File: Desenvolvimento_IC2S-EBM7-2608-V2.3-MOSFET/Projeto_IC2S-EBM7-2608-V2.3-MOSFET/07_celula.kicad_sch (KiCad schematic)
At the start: 23 parts, among them U13 LP5907MFX-2.5

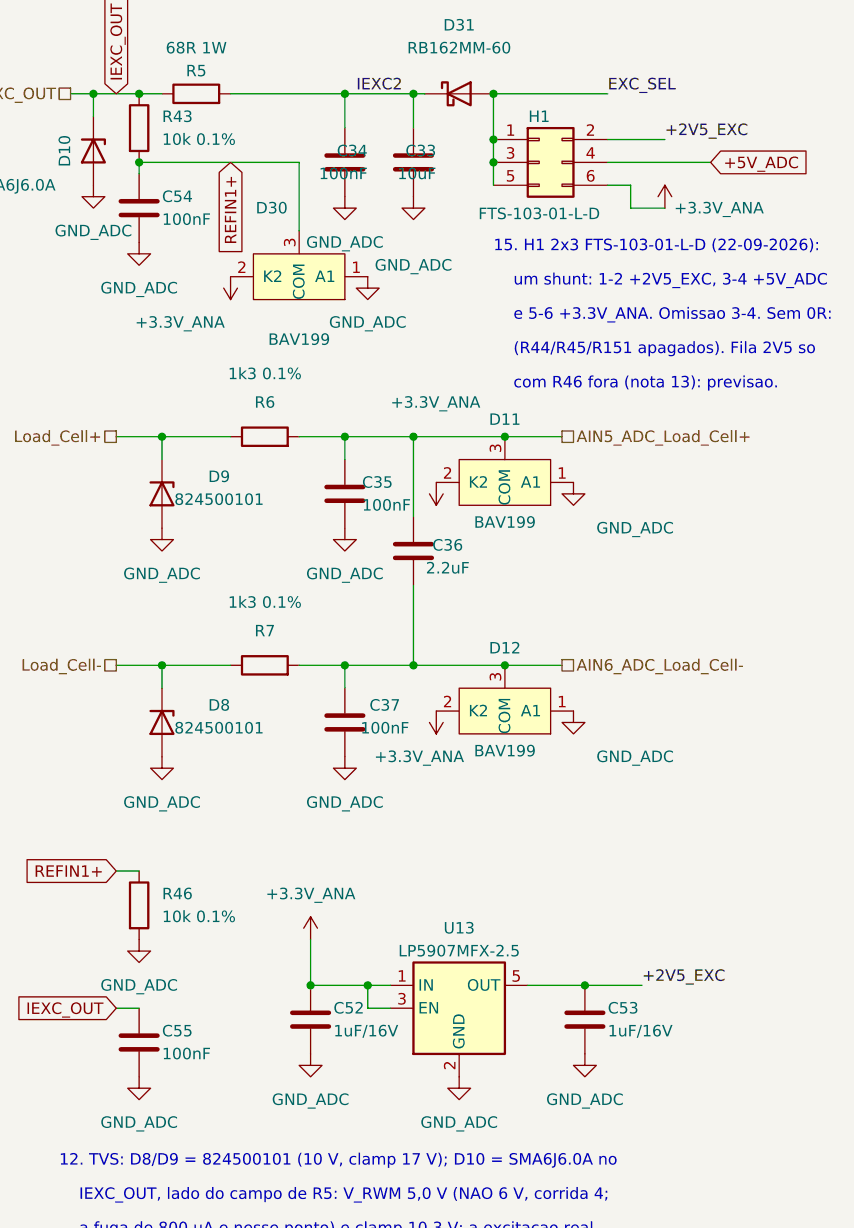
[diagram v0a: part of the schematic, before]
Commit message: Revisao da reuniao 28-09: ramo unico de 24 V, 100 nF a 50 V, um so MPN de 1 uF
- Saem F2, o diodo e o condensador do ramo +24V_ADC; F1 + diodo alimentam o
  R-78HB e o +24V_ADC. +24V_REG deixa de existir (esquematico, PCB, netclasses).
- Condensador de entrada do R-78HB conferido contra o datasheet Recom (p.4):
  10 uF/100 V cumpre os 3,3 uF/100 V pedidos com Vin > 50 V. Sem alteracao.
- 100 nF fora do 24 V -> TDK C1608X7R1H104K080AA (50 V); o do +24V_ADC fica
  GRM188R72A104KA35D (100 V). 1 uF -> TDK C1608X7R1H105K080AB nos quatro.
- Notas 2, 13 e 14 da folha 2; README e registo em 00-Especificacoes;
  catalogo TDK em Documentos_de_Referencia.

Co-Authored-By: Claude Opus 5.5 (1M context) <noreply@anthropic.com>
Claude-Session: https://claude.ai/code/session_01KPnkiJQKrkjgRqqw9M78ie
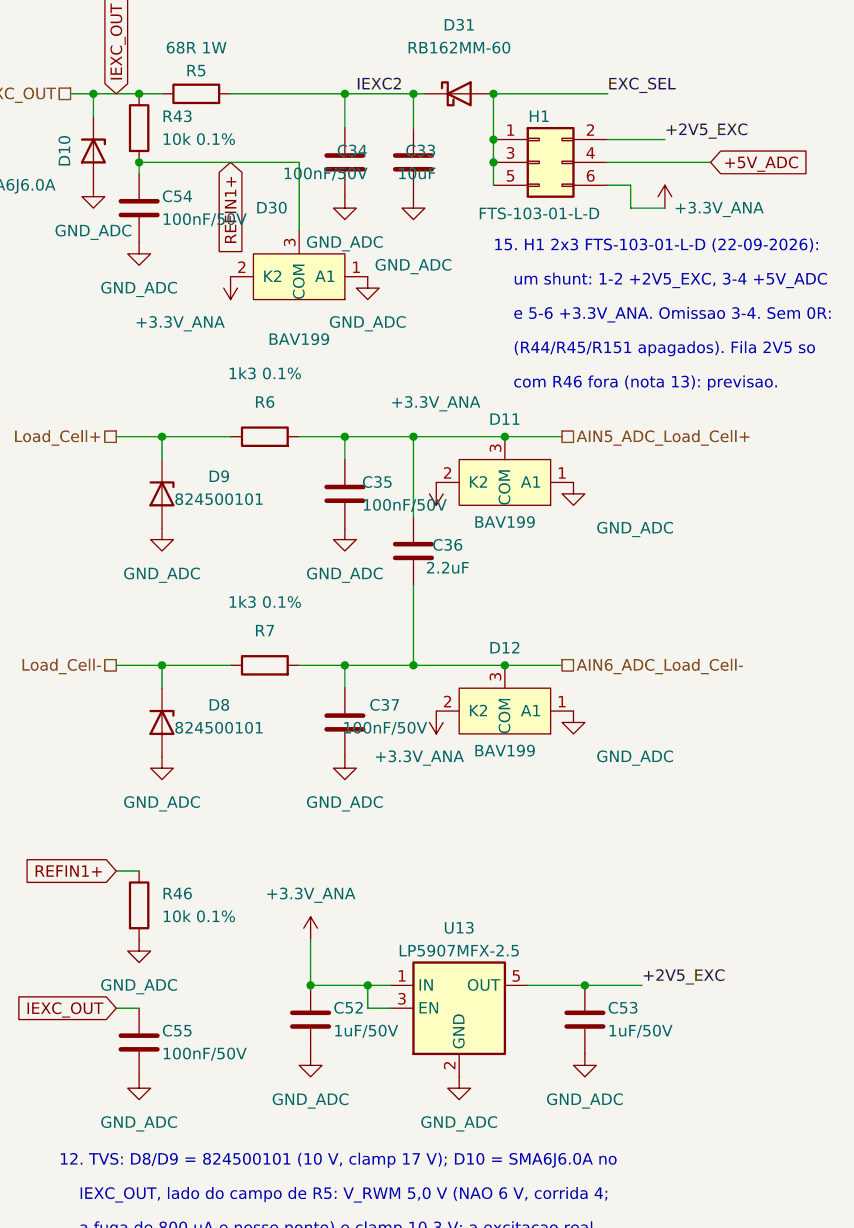
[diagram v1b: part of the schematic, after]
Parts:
- C34, C35, C37, C54, C55: value 100nF -> 100nF/50V; MPN GRM188R72A104KA35D -> C1608X7R1H104K080AA
- C52, C53: value 1uF/16V -> 1uF/50V; MPN C0603C105K4RACTU -> C1608X7R1H105K080AB
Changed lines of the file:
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@@
 			)
 		)
-		(property "Value" "1uF/16V"
+		(property "Value" "1uF/50V"
 			(at 54.61 152.4 0)
 			(show_name no)
@@
 			)
 		)
-		(property "MPN" "C0603C105K4RACTU"
+		(property "MPN" "C1608X7R1H105K080AB"
 			(at 52.07 151.13 0)
 			(hide yes)
@@
 			)
 		)
-		(property "Value" "100nF"
+		(property "Value" "100nF/50V"
 			(at 35.56 62.23 0)
 			(show_name no)
@@
 			)
 		)
-		(property "MPN" "GRM188R72A104KA35D"
+		(property "MPN" "C1608X7R1H104K080AA"
 			(at 33.02 60.96 0)
 			(hide yes)
@@
 			)
 		)
-		(property "Value" "100nF"
+		(property "Value" "100nF/50V"
 			(at 60.325 118.745 0)
 			(show_name no)
@@
 			)
 		)
-		(property "MPN" "GRM188R72A104KA35D"
+		(property "MPN" "C1608X7R1H104K080AA"
 			(at 0 0 0)
 			(hide yes)
@@
 			)
 		)
-		(property "Value" "100nF"
+		(property "Value" "100nF/50V"
 			(at 35.56 154.94 0)
 			(show_name no)
@@
 			)
 		)
-		(property "MPN" "GRM188R72A104KA35D"
+		(property "MPN" "C1608X7R1H104K080AA"
 			(at 33.02 153.67 0)
 			(hide yes)
@@
 			)
 		)
-		(property "Value" "1uF/16V"
+		(property "Value" "1uF/50V"
 			(at 85.09 152.4 0)
 			(show_name no)
@@
 			)
 		)
-		(property "MPN" "C0603C105K4RACTU"
+		(property "MPN" "C1608X7R1H105K080AB"
 			(at 82.55 151.13 0)
 			(hide yes)
@@
 			)
 		)
-		(property "Value" "100nF"
+		(property "Value" "100nF/50V"
 			(at 58.42 57.15 0)
 			(show_name no)
@@
 			)
 		)
-		(property "MPN" "GRM188R72A104KA35D"
+		(property "MPN" "C1608X7R1H104K080AA"
 			(at -22.86 0 0)
 			(hide yes)
@@
 			)
 		)
-		(property "Value" "100nF"
+		(property "Value" "100nF/50V"
 			(at 57.79 93.98 0)
 			(show_name no)
@@
 			)
 		)
-		(property "MPN" "GRM188R72A104KA35D"
+		(property "MPN" "C1608X7R1H104K080AA"
 			(at 0 0 0)
 			(hide yes)
